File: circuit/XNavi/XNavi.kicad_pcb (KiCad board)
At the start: 2 copper layers, 0 parts

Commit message: 回路図&PCBを追加
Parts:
- added C10: 0.1u, Capacitor_SMD:C_0603_1608Metric_Pad1.08x0.95mm_HandSolder, F.Cu at (47.1, 53.7)
- added C11: 0.1u, Capacitor_SMD:C_0603_1608Metric_Pad1.08x0.95mm_HandSolder, F.Cu at (52.6, 47.9)
- added C12: 0.1u, Capacitor_SMD:C_0603_1608Metric_Pad1.08x0.95mm_HandSolder, F.Cu at (46.5, 35.6)
- added C13: 0.1u, Capacitor_SMD:C_0603_1608Metric_Pad1.08x0.95mm_HandSolder, F.Cu at (33.0, 41.4)
- added C14: 0.1u, Capacitor_SMD:C_0603_1608Metric_Pad1.08x0.95mm_HandSolder, F.Cu at (61.2, 40.5)
- added C15: 0.1u, Capacitor_SMD:C_0603_1608Metric_Pad1.08x0.95mm_HandSolder, F.Cu at (58.4, 56.7)
- added C2: 0.1u, Capacitor_SMD:C_0603_1608Metric_Pad1.08x0.95mm_HandSolder, F.Cu at (49.2, 60.4)
- added C3: 1.0u, Capacitor_SMD:C_0603_1608Metric_Pad1.08x0.95mm_HandSolder, F.Cu at (55.1, 62.2)
- added C4: 2.2p, Capacitor_SMD:C_0603_1608Metric_Pad1.08x0.95mm_HandSolder, B.Cu at (28.4, 51.5)
- added C5: 2.2p, Capacitor_SMD:C_0603_1608Metric_Pad1.08x0.95mm_HandSolder, B.Cu at (33.8, 56.9)
- added C6: 2.2u, Capacitor_SMD:C_0603_1608Metric_Pad1.08x0.95mm_HandSolder, F.Cu at (51.4, 49.1)
- added C7: 2.2u, Capacitor_SMD:C_0603_1608Metric_Pad1.08x0.95mm_HandSolder, F.Cu at (34.5, 39.9)
- added C8: 0.1u, Capacitor_SMD:C_0603_1608Metric_Pad1.08x0.95mm_HandSolder, F.Cu at (34.0, 48.1)
- added C9: 0.1u, Capacitor_SMD:C_0603_1608Metric_Pad1.08x0.95mm_HandSolder, F.Cu at (38.3, 52.4)
- added D3: LED, LED_SMD:LED_0603_1608Metric_Pad1.05x0.95mm_HandSolder, F.Cu at (67.8, 33.8)
- added D4: LED, Diode_SMD:D_0603_1608Metric_Pad1.05x0.95mm_HandSolder, F.Cu at (65.2, 60.7)
- added D5: LED, Diode_SMD:D_0603_1608Metric_Pad1.05x0.95mm_HandSolder, F.Cu at (65.3, 57.8)
- added G***: LOGO, AIOLIA:AIOLIA, F.Cu at (24.8, 59.7)
- added J3: Micro_SD_Card_Det_Hirose_DM3AT, Connector_Card:microSD_HC_Hirose_DM3D-SF, F.Cu at (34.6, 27.0)
- added J4: Conn_01x02, Connector_JST:JST_PH_B2B-PH-SM4-TB_1x02-1MP_P2.00mm_Vertical, F.Cu at (40.8, 65.1)
- added J5: Conn_ST_STDC14, AIOLIA:CONN14_3220-14_CNC, F.Cu at (46.7, 22.6)
- added J6: Conn_01x04, Connector_JST:JST_PH_S4B-PH-SM4-TB_1x04-1MP_P2.00mm_Horizontal, F.Cu at (64.8, 48.5)
- added J7: Conn_02x03_Odd_Even, Connector_PinHeader_2.54mm:PinHeader_2x03_P2.54mm_Vertical, F.Cu at (33.5, 68.1)
- added J9: Conn_Coaxial, Connector_Coaxial:U.FL_Molex_MCRF_73412-0110_Vertical, F.Cu at (66.6, 25.2)
- added JP1: Jumper_2_Open, Jumper:SolderJumper-2_P1.3mm_Open_RoundedPad1.0x1.5mm, F.Cu at (52.2, 66.2)
- added L1: 27n, Inductor_SMD:L_0805_2012Metric_Pad1.15x1.40mm_HandSolder, F.Cu at (60.5, 23.2)
- added R1: 10k, Resistor_SMD:R_0603_1608Metric_Pad0.98x0.95mm_HandSolder, B.Cu at (39.9, 32.2)
- added R10: 10k (DNP), Resistor_SMD:R_0603_1608Metric_Pad0.98x0.95mm_HandSolder, B.Cu at (41.5, 45.5)
- added R11: 10k, Resistor_SMD:R_0603_1608Metric_Pad0.98x0.95mm_HandSolder, B.Cu at (39.1, 44.4)
- added R12: 10k, Resistor_SMD:R_0603_1608Metric_Pad0.98x0.95mm_HandSolder, B.Cu at (35.4, 51.1)
- added R13: 120, Resistor_SMD:R_0603_1608Metric_Pad0.98x0.95mm_HandSolder, B.Cu at (62.0, 50.5)
- added R14: 10, Resistor_SMD:R_0603_1608Metric_Pad0.98x0.95mm_HandSolder, F.Cu at (59.5, 25.9)
- added R15: 200, Resistor_SMD:R_0603_1608Metric_Pad0.98x0.95mm_HandSolder, F.Cu at (66.8, 36.4)
- added R16: 200, Resistor_SMD:R_0603_1608Metric_Pad0.98x0.95mm_HandSolder, B.Cu at (65.2, 60.7)
- added R17: 200, Resistor_SMD:R_0603_1608Metric_Pad0.98x0.95mm_HandSolder, B.Cu at (65.3, 57.8)
- added R2: 10k, Resistor_SMD:R_0603_1608Metric_Pad0.98x0.95mm_HandSolder, B.Cu at (39.9, 30.7)
- added R3: 10k, Resistor_SMD:R_0603_1608Metric_Pad0.98x0.95mm_HandSolder, B.Cu at (39.9, 29.2)
- added R4: 10k, Resistor_SMD:R_0603_1608Metric_Pad0.98x0.95mm_HandSolder, B.Cu at (28.1, 30.7)
- added R5: 10k, Resistor_SMD:R_0603_1608Metric_Pad0.98x0.95mm_HandSolder, B.Cu at (28.1, 32.2)
- added R6: 10k, Resistor_SMD:R_0603_1608Metric_Pad0.98x0.95mm_HandSolder, B.Cu at (41.9, 23.1)
- added SW1: SW_Slide, AIOLIA:SW_Slide, F.Cu at (41.8, 58.3)
- added SW2: SW_Push, Button_Switch_SMD:SW_Push_1P1T_NO_6x6mm_H9.5mm, F.Cu at (25.3, 40.2)
- added U2: ~, AIOLIA:SOT95P280X130-5N, F.Cu at (52.3, 62.0)
- added U3: STM32H573RITx, Package_QFP:LQFP-64_10x10mm_P0.5mm, F.Cu at (42.9, 44.5)
- added U4: ~, Package_TO_SOT_SMD:SOT-23-8_Handsoldering, B.Cu at (55.5, 46.7)
- added U5: ASM330LHHTR, Package_LGA:LGA-14_3x2.5mm_P0.5mm_LayoutBorder3x4y, F.Cu at (54.7, 56.0)
- added U6: MAX-M10S, RF_GPS:ublox_MAX, F.Cu at (59.3, 33.8)
- added Y1: 16MHz, Crystal:Crystal_HC52-U_Vertical, F.Cu at (31.1, 51.5)
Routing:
- net +3V3: track 0.00 -> 210.6 mm, vias 0 -> 7
- net Net-(J6-Pin_4): track 0.00 -> 32.5 mm
- net SDIO_DAT0: track 0.00 -> 31.0 mm, vias 0 -> 3
- net SDIO_DAT1: track 0.00 -> 26.0 mm, vias 0 -> 2
- net VCC: track 0.00 -> 25.0 mm
- net RST: track 0.00 -> 24.9 mm, vias 0 -> 2
- net PPS: track 0.00 -> 24.4 mm
- net RX1: track 0.00 -> 23.4 mm, vias 0 -> 1
- net LED0: track 0.00 -> 22.7 mm, vias 0 -> 1
- net SD_DET: track 0.00 -> 21.0 mm, vias 0 -> 1
- net LED1: track 0.00 -> 20.5 mm, vias 0 -> 1
- net GND: track 0.00 -> 20.5 mm, vias 0 -> 94
- net AIN0: track 0.00 -> 20.4 mm, vias 0 -> 1
- net AIN1: track 0.00 -> 18.9 mm, vias 0 -> 1
- net TX1: track 0.00 -> 18.8 mm
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- added copper zone on B.Cu, net GND
- added copper zone on F.Cu, net GND
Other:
- board outline added: 50 x 50 mm
- board text added: "3v3"
- board text added: "AIN0"
- board text added: "AIN1"
- board text added: "GND"
- board text added: "XNavi"

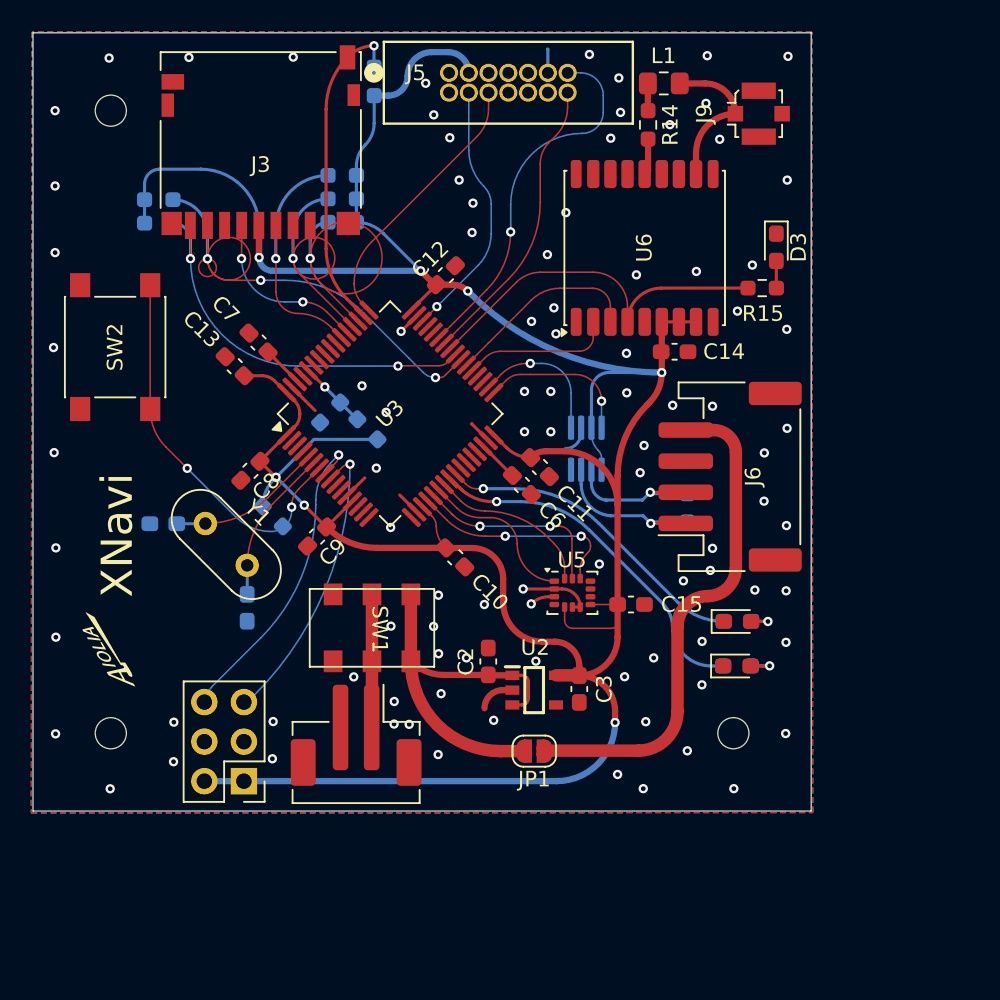
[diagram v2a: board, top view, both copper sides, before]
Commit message: MCUをRaspberry Pi Pico(2)に変更
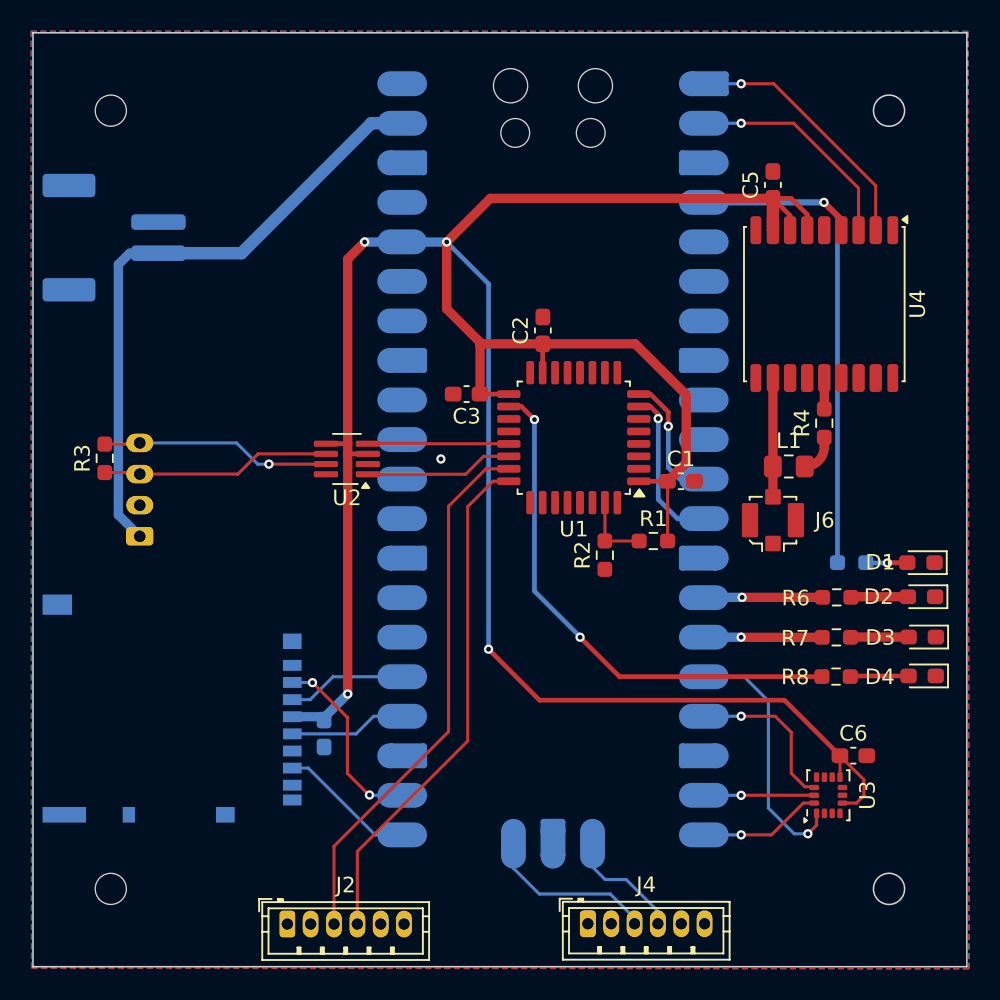
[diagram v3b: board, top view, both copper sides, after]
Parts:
- removed C10, C11, C12, C13, C14, C15, C8, C9: 0.1u, Capacitor_SMD:C_0603_1608Metric_Pad1.08x0.95mm_HandSolder
- removed C7: 2.2u, Capacitor_SMD:C_0603_1608Metric_Pad1.08x0.95mm_HandSolder
- removed D5: LED, Diode_SMD:D_0603_1608Metric_Pad1.05x0.95mm_HandSolder
- removed G***: LOGO, AIOLIA:AIOLIA
- removed J7: Conn_02x03_Odd_Even, Connector_PinHeader_2.54mm:PinHeader_2x03_P2.54mm_Vertical
- removed J9: Conn_Coaxial, Connector_Coaxial:U.FL_Molex_MCRF_73412-0110_Vertical
- removed JP1: Jumper_2_Open, Jumper:SolderJumper-2_P1.3mm_Open_RoundedPad1.0x1.5mm
- removed R10: 10k (DNP), Resistor_SMD:R_0603_1608Metric_Pad0.98x0.95mm_HandSolder
- removed R11, R12: 10k, Resistor_SMD:R_0603_1608Metric_Pad0.98x0.95mm_HandSolder
- removed R13: 120, Resistor_SMD:R_0603_1608Metric_Pad0.98x0.95mm_HandSolder
- removed R14: 10, Resistor_SMD:R_0603_1608Metric_Pad0.98x0.95mm_HandSolder
- removed R15, R16, R17: 200, Resistor_SMD:R_0603_1608Metric_Pad0.98x0.95mm_HandSolder
- removed SW1: SW_Slide, AIOLIA:SW_Slide
- removed SW2: SW_Push, Button_Switch_SMD:SW_Push_1P1T_NO_6x6mm_H9.5mm
- removed U5: ASM330LHHTR, Package_LGA:LGA-14_3x2.5mm_P0.5mm_LayoutBorder3x4y
- removed U6: MAX-M10S, RF_GPS:ublox_MAX
- removed Y1: 16MHz, Crystal:Crystal_HC52-U_Vertical
- added A1: RaspberryPi_Pico, Module:RaspberryPi_Pico_SMD_HandSolder, B.Cu at (53.4, 47.4)
- added C1: 0.1u, Capacitor_SMD:C_0603_1608Metric_Pad1.08x0.95mm_HandSolder, F.Cu at (61.6, 48.8)
- added D1: LED, LED_SMD:LED_0603_1608Metric_Pad1.05x0.95mm_HandSolder, F.Cu at (77.0, 54.0)
- added D2: LED, Diode_SMD:D_0603_1608Metric_Pad1.05x0.95mm_HandSolder, F.Cu at (77.1, 56.2)
- added J1: Micro_SD_Card_Det, Connector_Card:microSD_HC_Hirose_DM3AT-SF-PEJM5, B.Cu at (28.9, 63.4)
- added J2: Conn_01x06, Connector_JST:JST_ZH_B6B-ZR_1x06_P1.50mm_Vertical, F.Cu at (36.3, 77.3)
- added R7: 200, Resistor_SMD:R_0603_1608Metric_Pad0.98x0.95mm_HandSolder, F.Cu at (71.6, 58.8)
- added R8: 200, Resistor_SMD:R_0603_1608Metric_Pad0.98x0.95mm_HandSolder, F.Cu at (71.6, 61.4)
- added U1: STM32G441KBTx, Package_QFP:LQFP-32_7x7mm_P0.8mm, F.Cu at (54.7, 46.0)
- C3: value 1.0u -> 0.1u
- C4: value 2.2p -> 0.1u
- C5: value 2.2p -> 0.1u; moved to F.Cu
- C6: value 2.2u -> 0.1u
- D3: footprint LED_SMD:LED_0603_1608Metric_Pad1.05x0.95mm_HandSolder -> Diode_SMD:D_0603_1608Metric_Pad1.05x0.95mm_HandSolder
- J3: value Micro_SD_Card_Det_Hirose_DM3AT -> Conn_01x04; footprint Connector_Card:microSD_HC_Hirose_DM3D-SF -> Connector_JST:JST_PH_S4B-PH-K_1x04_P2.00mm_Horizontal; moved to B.Cu
- J4: value Conn_01x02 -> Conn_01x06; footprint Connector_JST:JST_PH_B2B-PH-SM4-TB_1x02-1MP_P2.00mm_Vertical -> Connector_JST:JST_ZH_B6B-ZR_1x06_P1.50mm_Vertical
- J5: value Conn_ST_STDC14 -> Conn_01x02; footprint AIOLIA:CONN14_3220-14_CNC -> Connector_JST:JST_PH_S2B-PH-SM4-TB_1x02-1MP_P2.00mm_Horizontal; moved to B.Cu
- J6: value Conn_01x04 -> Conn_Coaxial; footprint Connector_JST:JST_PH_S4B-PH-SM4-TB_1x04-1MP_P2.00mm_Horizontal -> Connector_Coaxial:U.FL_Molex_MCRF_73412-0110_Vertical
- R1, R2: value 10k -> 100; moved to F.Cu
- R3: value 10k -> 120; moved to F.Cu
- R4: value 10k -> 10; moved to F.Cu
- R5: value 10k -> 200
- R6: value 10k -> 200; moved to F.Cu
- U2: footprint AIOLIA:SOT95P280X130-5N -> Package_TO_SOT_SMD:SOT-23-8_Handsoldering
- U3: value STM32H573RITx -> ASM330LHHTR; footprint Package_QFP:LQFP-64_10x10mm_P0.5mm -> Package_LGA:LGA-14_3x2.5mm_P0.5mm_LayoutBorder3x4y
- U4: value ~ -> MAX-M10S; footprint Package_TO_SOT_SMD:SOT-23-8_Handsoldering -> RF_GPS:ublox_MAX; moved to F.Cu
- moved R5 49.6 mm to (72.6, 54.0), turned to 0 degrees
- moved R4 45.1 mm to (70.8, 45.1), turned to 90 degrees
- moved R6 44.5 mm to (71.6, 56.3), turned to 0 degrees
- moved C5 43.4 mm to (67.5, 29.8)
- moved U3 37.3 mm to (71.1, 69.0), turned to 90 degrees
- moved R1 28.6 mm to (59.9, 52.6)
- moved R2 28.4 mm to (56.7, 53.6), turned to 90 degrees
- moved C6 27.5 mm to (72.7, 66.4), turned to 0 degrees
- moved D3 26.7 mm to (77.1, 58.8), turned to 180 degrees
- moved J3 26.5 mm to (26.9, 52.4), turned to 90 degrees
- moved L1 25.9 mm to (68.6, 47.9), turned to 0 degrees
- moved J5 24.0 mm to (25.2, 33.2), turned to 90 degrees
- moved R3 23.7 mm to (24.6, 47.3), turned to 90 degrees
- moved C2 21.6 mm to (52.8, 39.1)
- moved C3 20.3 mm to (47.9, 43.2), turned to 180 degrees
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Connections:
- C2 pad 1: VCC -> +3V3
- C3 pad 1: GND -> +3V3
- C3 pad 2: +3V3 -> GND
- C4 pad 2: Net-(U3-PH0) -> +3V3
- C5 pad 1: GND -> +3V3
- C5 pad 2: Net-(U3-PH1) -> GND
- C6 pad 1: Net-(C6-Pad1) -> +3V3
- J3 pad 1: SDIO_DAT2 -> VCC
- J3 pad 2: SDIO_DAT3 -> GND
- J3 pad 3: SDIO_CMD -> /CAN-
- J3 pad 4: +3V3 -> /CAN+
- J4 pad 1: Net-(J4-Pin_1) -> unconnected-(J4-Pin_1-Pad1)
- J4 pad 2: GND -> unconnected-(J4-Pin_2-Pad2)
- J5 pad 1: unconnected-(J5-NC-Pad1) -> VCC
- J5 pad 2: unconnected-(J5-NC-Pad2) -> GND
- J6 pad 1: Net-(J6-Pin_1) -> /RF
- J6 pad 2: Net-(J6-Pin_2) -> GND
- R1 pad 1: SDIO_DAT2 -> /BOOT0
- R2 pad 1: SDIO_DAT3 -> GND
- R2 pad 2: +3V3 -> /BOOT0
- R3 pad 1: SDIO_CMD -> /CAN-
- R3 pad 2: +3V3 -> /CAN+
- R4 pad 1: SDIO_DAT0 -> Net-(L1-Pad2)
- R4 pad 2: +3V3 -> Net-(U4-VCC_RF)
- R5 pad 1: SDIO_DAT1 -> PPS
- R5 pad 2: +3V3 -> Net-(D1-A)
- R6 pad 1: SD_DET -> LED0
- R6 pad 2: +3V3 -> Net-(D2-A)
- U2 pad 1: VCC -> CAN_TX
- U2 pad 3: VCC -> +3V3
- U2 pad 4: unconnected-(U2-NC-Pad4) -> CAN_RX
- U3 pad 1: +3V3 -> SPI1_MISO
- U3 pad 10: AIN2 -> unconnected-(U3-NC-Pad10)
- U3 pad 11: AIN3 -> unconnected-(U3-NC-Pad11)
- U3 pad 12: GND -> SPI1_CS
- U3 pad 13: +3V3 -> SPI1_SCK
- U3 pad 14: unconnected-(U3-PA0-Pad14) -> SPI1_MOSI
- U3 pad 2: SW -> GND
- U3 pad 3: LED2 -> GND
- U3 pad 4: LED3 -> unconnected-(U3-INT1-Pad4)
- U3 pad 5: Net-(U3-PH0) -> +3V3
- U3 pad 6: Net-(U3-PH1) -> GND
- U3 pad 7: RST -> GND
- U3 pad 8: AIN0 -> +3V3
- U3 pad 9: AIN1 -> unconnected-(U3-INT2-Pad9)
- U4 pad 1: FDCAN2_TX -> GND
- U4 pad 2: GND -> TX1
- U4 pad 3: +3V3 -> RX1
- U4 pad 4: FDCAN2_RX -> PPS
- U4 pad 5: +3V3 -> unconnected-(U4-EXTINT-Pad5)
- U4 pad 6: Net-(J6-Pin_2) -> +3V3
- U4 pad 7: Net-(J6-Pin_1) -> +3V3
- U4 pad 8: GND -> +3V3
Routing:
- net +3V3: track 210.6 -> 171.5 mm, vias 7 -> 4
- net SWDIO_STM32: track 0.00 -> 34.8 mm
- net LED2: track 0.00 -> 33.8 mm, vias 0 -> 2
- net SWCLK_STM32: track 0.00 -> 33.1 mm
- net Net-(J6-Pin_4): track 32.5 -> 0.00 mm
- net SDIO_DAT0: track 31.0 -> 0.00 mm, vias 3 -> 0
- net SDIO_DAT1: track 26.0 -> 0.00 mm, vias 2 -> 0
- net RST: track 24.9 -> 0.00 mm, vias 2 -> 0
- net SD_DET: track 21.0 -> 0.00 mm, vias 1 -> 0
- net GND: track 20.5 -> 0.00 mm, vias 94 -> 1
- net AIN0: track 20.4 -> 0.00 mm, vias 1 -> 0
- net AIN1: track 18.9 -> 0.00 mm, vias 1 -> 0
- net SDIO_CMD: track 16.8 -> 0.00 mm, vias 1 -> 0
- net LED0: track 22.7 -> 7.64 mm
- net VCC: track 25.0 -> 40.0 mm
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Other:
- board size 50 x 50 mm -> 60 x 60 mm
- board text removed: "3v3"
- board text removed: "AIN0"
- board text removed: "AIN1"
- board text removed: "GND"
- board text removed: "XNavi"

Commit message: RS485追加 & シルク追加
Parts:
- added G***: LOGO, AIOLIA:AIOLIA, F.Cu at (24.1, 30.7)
- added J7: Conn_01x04, Connector_JST:JST_PH_S4B-PH-SM4-TB_1x04-1MP_P2.00mm_Horizontal, B.Cu at (25.2, 47.6)
- added R9: 120, Resistor_SMD:R_0603_1608Metric_Pad0.98x0.95mm_HandSolder, B.Cu at (31.1, 49.7)
- added U5: MAX3485, Package_SO:SOP-8_3.76x4.96mm_P1.27mm, F.Cu at (40.2, 46.1)
- D1: footprint LED_SMD:LED_0603_1608Metric_Pad1.05x0.95mm_HandSolder -> Diode_SMD:D_0603_1608Metric_Pad1.05x0.95mm_HandSolder
- J3: footprint Connector_JST:JST_PH_S4B-PH-K_1x04_P2.00mm_Horizontal -> Connector_JST:JST_PH_S4B-PH-SM4-TB_1x04-1MP_P2.00mm_Horizontal; moved to F.Cu
- moved U2 10.1 mm to (40.2, 57.5)
- moved R3 6.93 mm to (31.1, 49.7), turned to -90 degrees
- moved J3 4.95 mm to (25.2, 47.7), turned to -90 degrees
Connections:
- U1 pad 19: unconnected-(U1-PA9-Pad19) -> TX1_STM32
- U1 pad 20: unconnected-(U1-PA10-Pad20) -> RX1_STM32
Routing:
- net Net-(J7-Pin_1): track 0.00 -> 11.2 mm, vias 0 -> 1
- net Net-(J7-Pin_2): track 0.00 -> 11.0 mm, vias 0 -> 1
- net RX1_STM32: track 0.00 -> 8.80 mm
- net TX1_STM32: track 0.00 -> 8.09 mm
- net CAN_TX: track 9.53 -> 17.3 mm
- net VCC: track 40.0 -> 33.7 mm, vias 0 -> 1
- net CAN_RX: track 9.05 -> 15.1 mm
- net +3V3: track 171.5 -> 174.0 mm
- net /CAN-: track 14.8 -> 15.7 mm
- net /CAN+: track 14.8 -> 15.2 mm, vias 1 -> 0
- net GND: vias 1 -> 40
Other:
- board text added: "A"
- board text added: "B"
- board text added: "CANH"
- board text added: "CANL"
- board text added: "GND"
- board text added: "RP2350"
- board text added: "STM32"
- board text added: "SWCLK"
- board text added: "SWDIO"
- board text added: "VCC"
- board text added: "X"
- board text added: "XNavi"
- board text added: "Y"
- board text added: "Z"
- board text added: "rev 2. - Adopt Raspberry Pi Pico 2 + STM32G441 - Changed the footprint of uSD card slot. designed by xsuz"
